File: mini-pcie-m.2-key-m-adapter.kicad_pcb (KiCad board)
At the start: 4 copper layers, 50 x 53.8 mm, 24 parts, among them J1 miniPCIe, J2 Bus_M.2_Socket_M

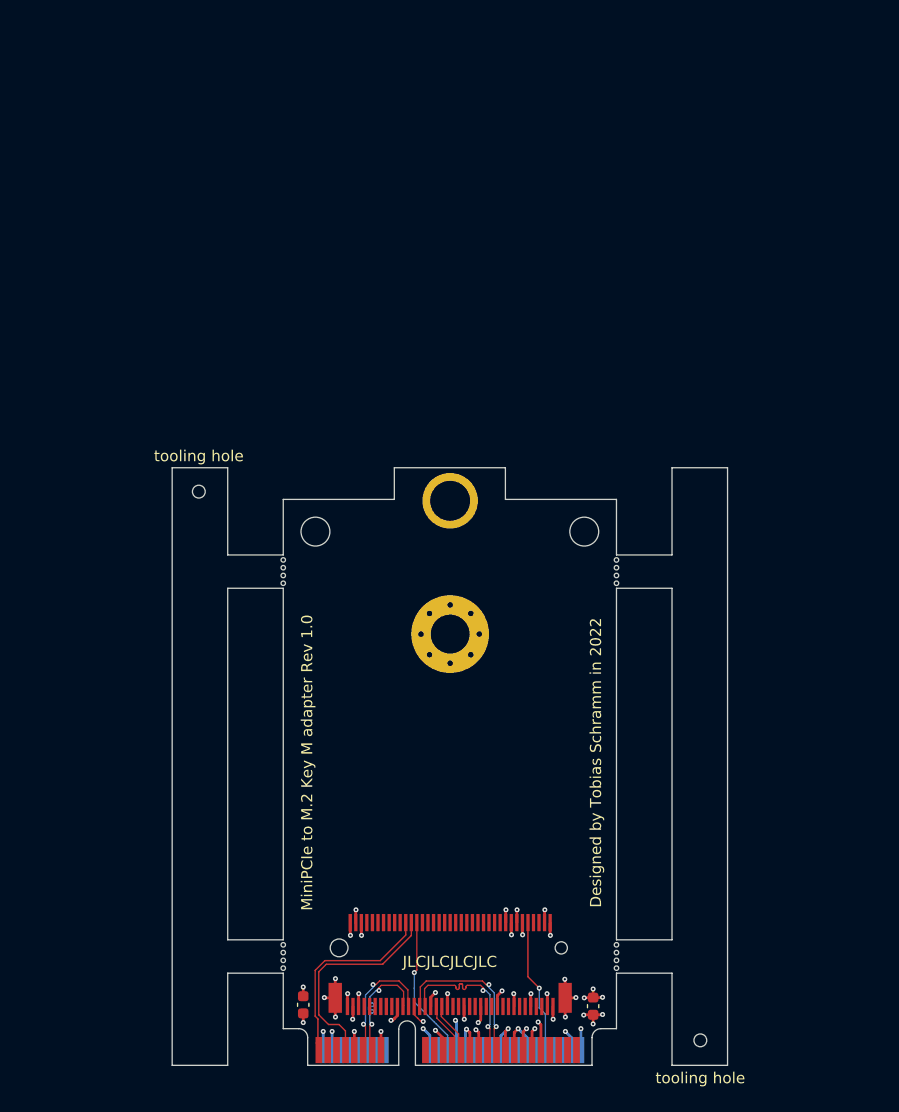
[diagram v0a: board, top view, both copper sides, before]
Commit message: Add 60mm and 90mm M.2 mounting options
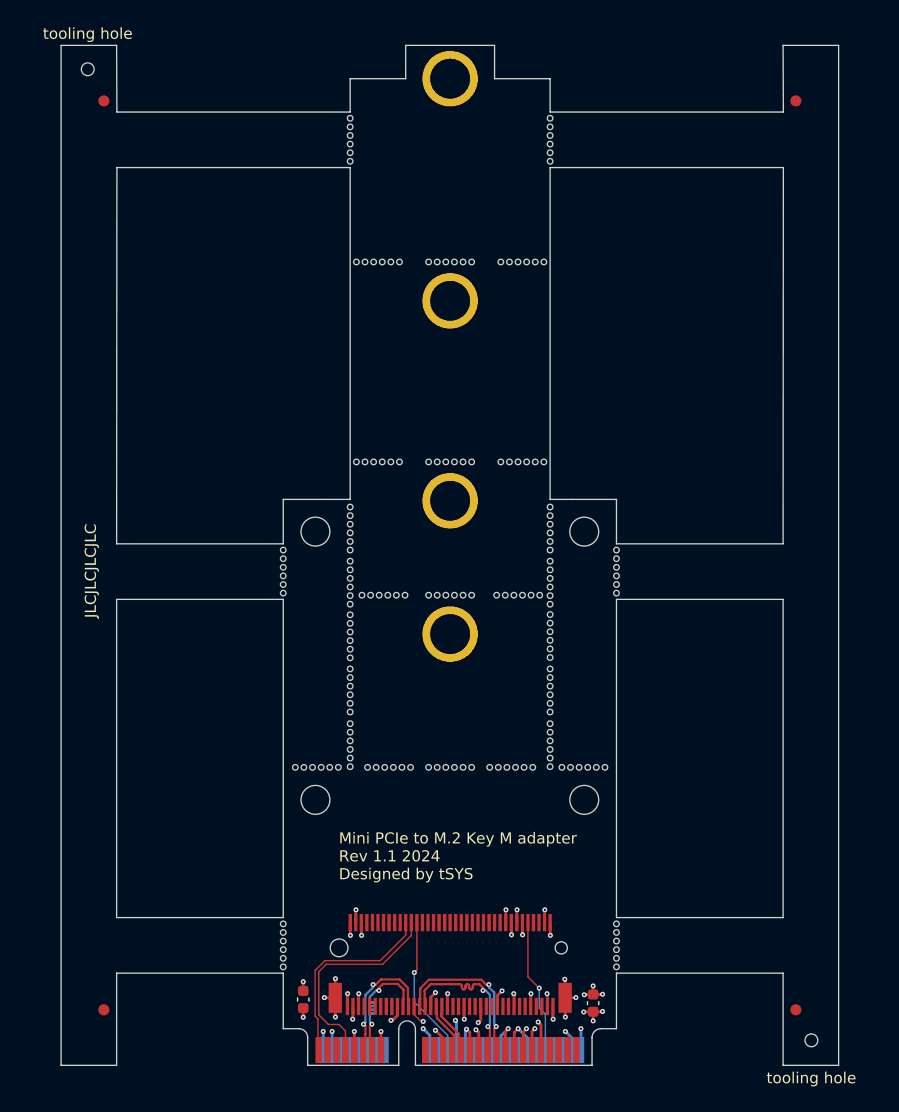
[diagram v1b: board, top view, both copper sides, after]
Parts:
- removed H1: MountingHole_Pad, MountingHole_small:MountingHole_3.6mm_small
- removed H10, H11, H12, H13, H14, H15, H16, H17, H18, H19, H20, H5, H6, H7, H8, H9: Perforation, Perforation:Perforation_0.4mm
- removed H4: MountingHole_Pad, MountingHole:MountingHole_3.5mm_Pad_Via
- added ?: , , F.Cu at (63.9, 29.2)
- added ?: , , F.Cu at (63.9, -8.82)
- added ?: , , F.Cu at (63.9, 11.2)
- added ?: , , F.Cu at (63.9, 41.2)
- added REF**: MouseBites_JLCSMT, ToolingHole:MouseBites_JLCSMT, F.Cu at (54.9, 36.5)
- added REF**: MouseBites_JLCSMT, ToolingHole:MouseBites_JLCSMT, F.Cu at (75.9, 53.2)
- added REF**: MouseBites_JLCSMT, ToolingHole:MouseBites_JLCSMT, F.Cu at (54.9, 31.7)
- added REF**: MouseBites_JLCSMT, ToolingHole:MouseBites_JLCSMT, F.Cu at (63.9, 7.67)
- added REF**: MouseBites_JLCSMT, ToolingHole:MouseBites_JLCSMT, F.Cu at (58.4, 53.2)
- added REF**: Fiducial_JLCSMT, ToolingHole:Fiducial_JLCSMT, F.Cu at (95.0, -6.82)
- added REF**: MouseBites_JLCSMT, ToolingHole:MouseBites_JLCSMT, F.Cu at (70.4, 25.7)
- added REF**: MouseBites_JLCSMT, ToolingHole:MouseBites_JLCSMT, F.Cu at (78.8, 69.2)
- added REF**: MouseBites_JLCSMT, ToolingHole:MouseBites_JLCSMT, F.Cu at (72.9, -3.33)
- added REF**: MouseBites_JLCSMT, ToolingHole:MouseBites_JLCSMT, F.Cu at (57.4, 7.67)
- added REF**: MouseBites_JLCSMT, ToolingHole:MouseBites_JLCSMT, F.Cu at (54.9, 51.2)
- added REF**: MouseBites_JLCSMT, ToolingHole:MouseBites_JLCSMT, F.Cu at (48.9, 35.5)
- added REF**: MouseBites_JLCSMT, ToolingHole:MouseBites_JLCSMT, F.Cu at (63.9, 53.2)
- added REF**: MouseBites_JLCSMT, ToolingHole:MouseBites_JLCSMT, F.Cu at (72.9, 36.5)
- added REF**: MouseBites_JLCSMT, ToolingHole:MouseBites_JLCSMT, F.Cu at (70.0, 37.7)
- added REF**: MouseBites_JLCSMT, ToolingHole:MouseBites_JLCSMT, F.Cu at (72.9, 31.7)
- added REF**: MouseBites_JLCSMT, ToolingHole:MouseBites_JLCSMT, F.Cu at (78.8, 35.5)
- added REF**: Fiducial_JLCSMT, ToolingHole:Fiducial_JLCSMT, F.Cu at (95.0, 75.0)
- added REF**: MouseBites_JLCSMT, ToolingHole:MouseBites_JLCSMT, F.Cu at (72.9, 46.2)
- added REF**: Fiducial_JLCSMT, ToolingHole:Fiducial_JLCSMT, F.Cu at (32.7, -6.83)
- added REF**: MouseBites_JLCSMT, ToolingHole:MouseBites_JLCSMT, F.Cu at (48.9, 69.2)
- added REF**: MouseBites_JLCSMT, ToolingHole:MouseBites_JLCSMT, F.Cu at (54.9, -3.33)
- added REF**: MouseBites_JLCSMT, ToolingHole:MouseBites_JLCSMT, F.Cu at (69.4, 53.2)
- added REF**: MouseBites_JLCSMT, ToolingHole:MouseBites_JLCSMT, F.Cu at (63.9, 37.7)
- added REF**: MouseBites_JLCSMT, ToolingHole:MouseBites_JLCSMT, F.Cu at (72.9, 51.2)
- added REF**: MouseBites_JLCSMT, ToolingHole:MouseBites_JLCSMT, F.Cu at (70.4, 7.67)
- added REF**: MouseBites_JLCSMT, ToolingHole:MouseBites_JLCSMT, F.Cu at (57.9, 37.7)
- added REF**: MouseBites_JLCSMT, ToolingHole:MouseBites_JLCSMT, F.Cu at (63.9, 25.7)
- added REF**: MouseBites_JLCSMT, ToolingHole:MouseBites_JLCSMT, F.Cu at (51.9, 53.2)
- added REF**: MouseBites_JLCSMT, ToolingHole:MouseBites_JLCSMT, F.Cu at (72.9, 41.4)
- added REF**: MouseBites_JLCSMT, ToolingHole:MouseBites_JLCSMT, F.Cu at (54.9, 46.2)
- added REF**: MouseBites_JLCSMT, ToolingHole:MouseBites_JLCSMT, F.Cu at (57.4, 25.7)
- added REF**: Fiducial_JLCSMT, ToolingHole:Fiducial_JLCSMT, F.Cu at (32.7, 75.0)
- added REF**: MouseBites_JLCSMT, ToolingHole:MouseBites_JLCSMT, F.Cu at (54.9, 41.4)
- moved H2 39.3 mm to (31.2, -9.68)
- moved H3 10.0 mm to (96.4, 77.8)
- moved C1 0.47 mm to (50.6, 74.1)
- moved C2 0.27 mm to (76.8, 74.4)
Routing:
- net /CLK-: track 11.5 -> 12.1 mm
- net /CLK+: track 11.5 -> 12.1 mm
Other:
- board size 50 x 53.8 mm -> 70 x 91.8 mm
- board text added: "Mini PCIe to M.2 Key M adapter Rev 1.1 2024 Designed by tSYS"
- board text removed: "Designed by Tobias Schramm in 2022"
- board text removed: "MiniPCIe to M.2 Key M adapter Rev 1.0"
